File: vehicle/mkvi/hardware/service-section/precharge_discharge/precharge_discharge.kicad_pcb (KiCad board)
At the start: 2 copper layers, 127 x 72.1 mm, 37 parts, among them J1 MicroFit_VT_5x1, J2 Automotive_M.2_Edge_Connector, K1 G2RG-2A-X_DC12, K2 3350-4275-126, Q1 SSM3K333R, U1 MCP6001, U2 MCP6001, U3 MCP6001

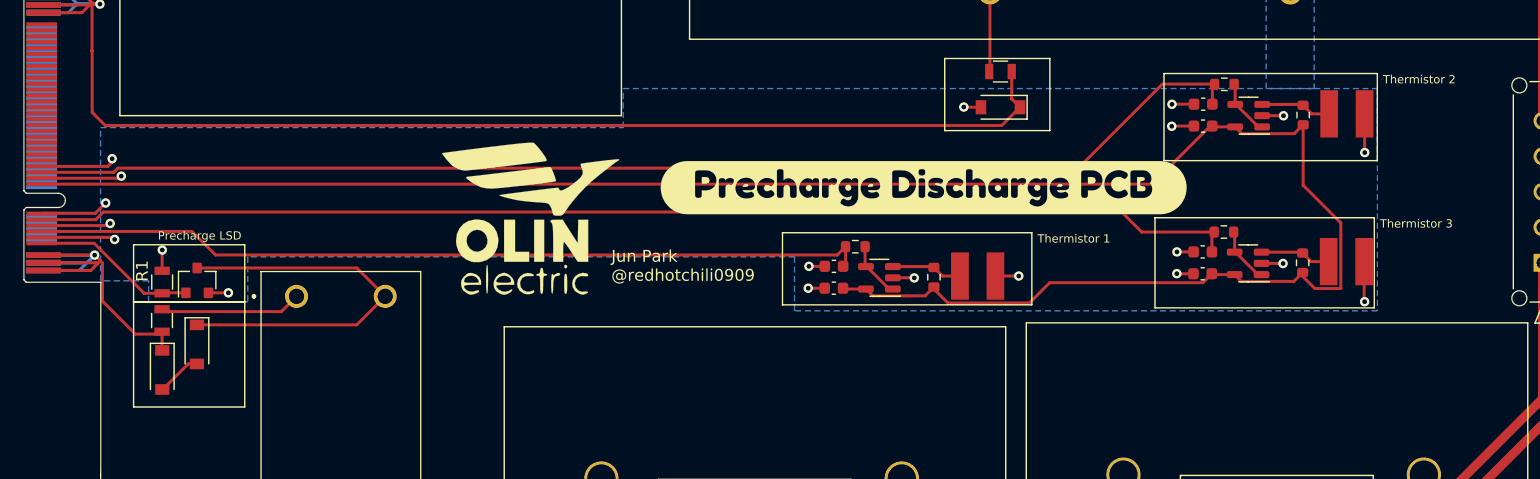
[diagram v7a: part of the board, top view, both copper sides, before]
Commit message: Added M.2 Mount Holes
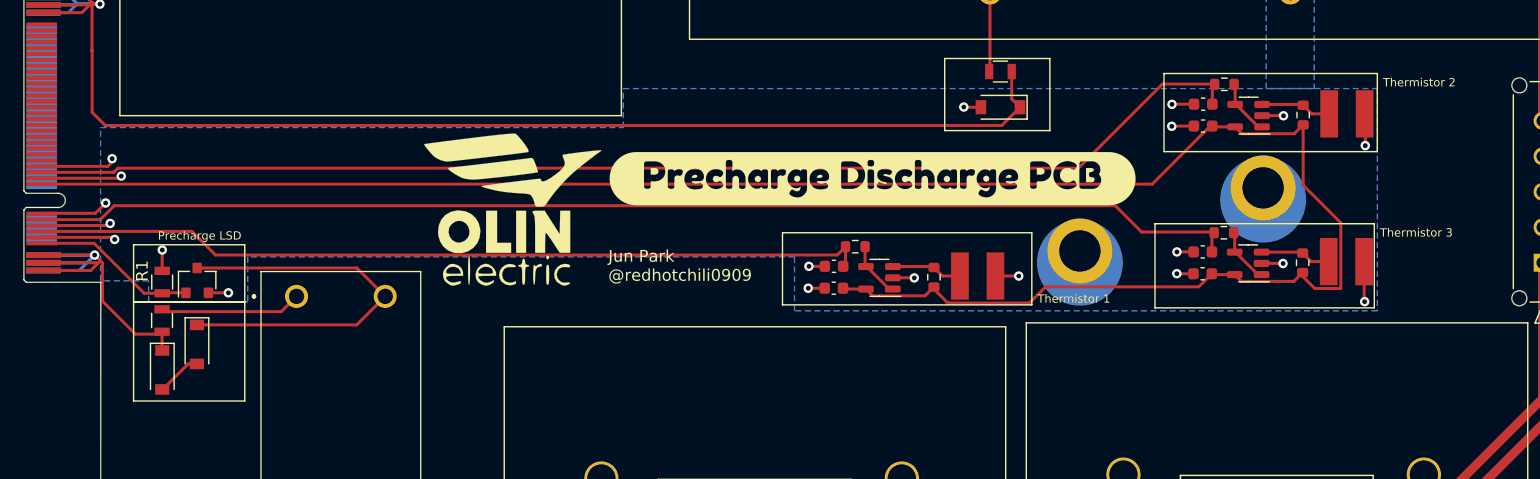
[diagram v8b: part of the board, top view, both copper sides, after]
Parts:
- added U$2: M.2_Mount, OEM:M.2_Mount, F.Cu at (164.3, 95.2)
- added U$2: M.2_Mount, OEM:M.2_Mount, F.Cu at (148.8, 100.6)
- moved G2 114.0 mm to (186.7, 127.3)
- moved G1 9.99 mm to (129.3, 110.2)
- moved kibuzzard-639639B8 4.38 mm to (131.3, 94.5)
- moved G3 2.98 mm to (105.9, 97.7)
- moved G*** 1.70 mm to (100.8, 97.0)
- moved R12 0.06 mm to (161.0, 99.1)
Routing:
- net GND: track 59.6 -> 59.0 mm
